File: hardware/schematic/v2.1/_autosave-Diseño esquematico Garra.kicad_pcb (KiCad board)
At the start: 2 copper layers, 85.5 x 137 mm, 26 parts

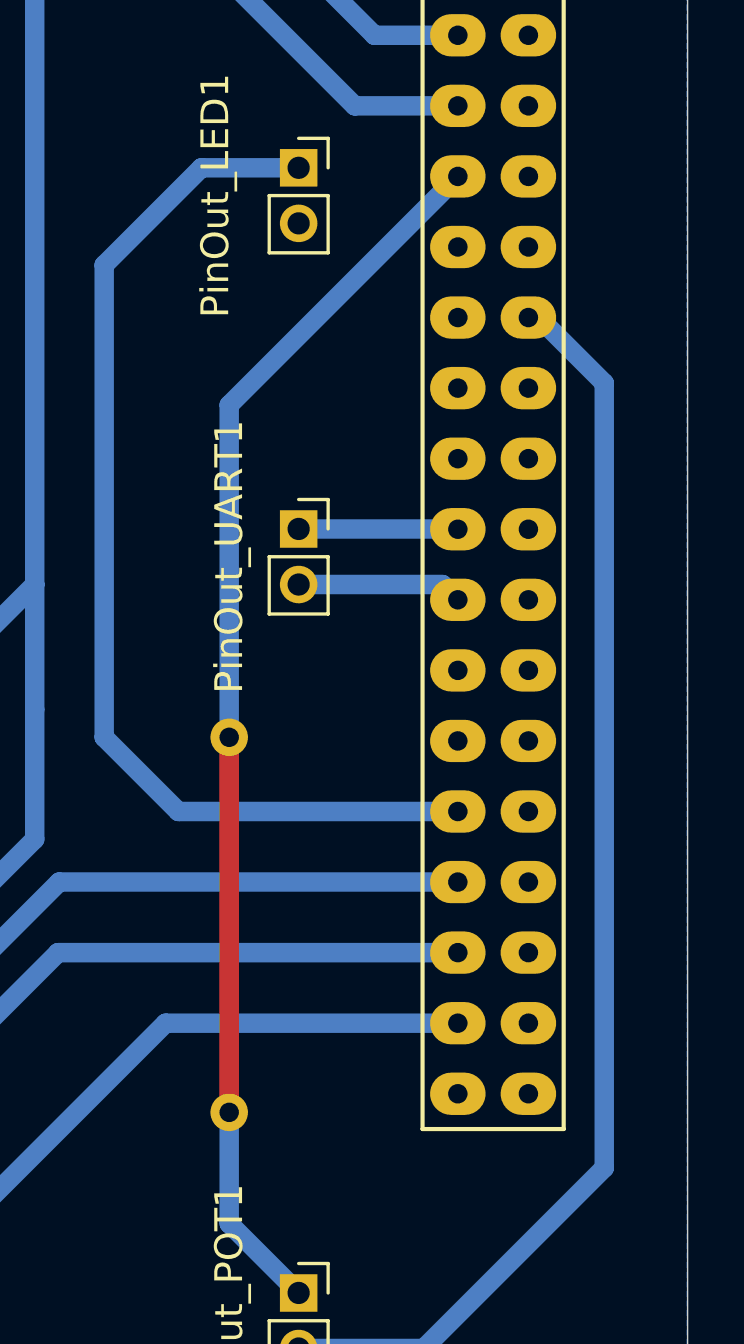
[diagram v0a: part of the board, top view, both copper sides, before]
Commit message: Pcb branch (#8)
* refactor

* feat: PCB routing first stage completed

* docs: Schematics PDF added

* fix: PCB border colision

* feat: Copper layers added to the PCB

* feat: New PCB design with new components [LED, B_M]

* feat: add through holes for connectivity & GNDs links

* feat: hole diameter adjustment

* fix: PDF

* feat: change route system in PCB

---------

Co-authored-by: ManuSavenia <saveniamanuel@egmail.com>
Co-authored-by: Iván Valentín Polanis <polanis.ivan@alu.ing.unlp.edu.ar>
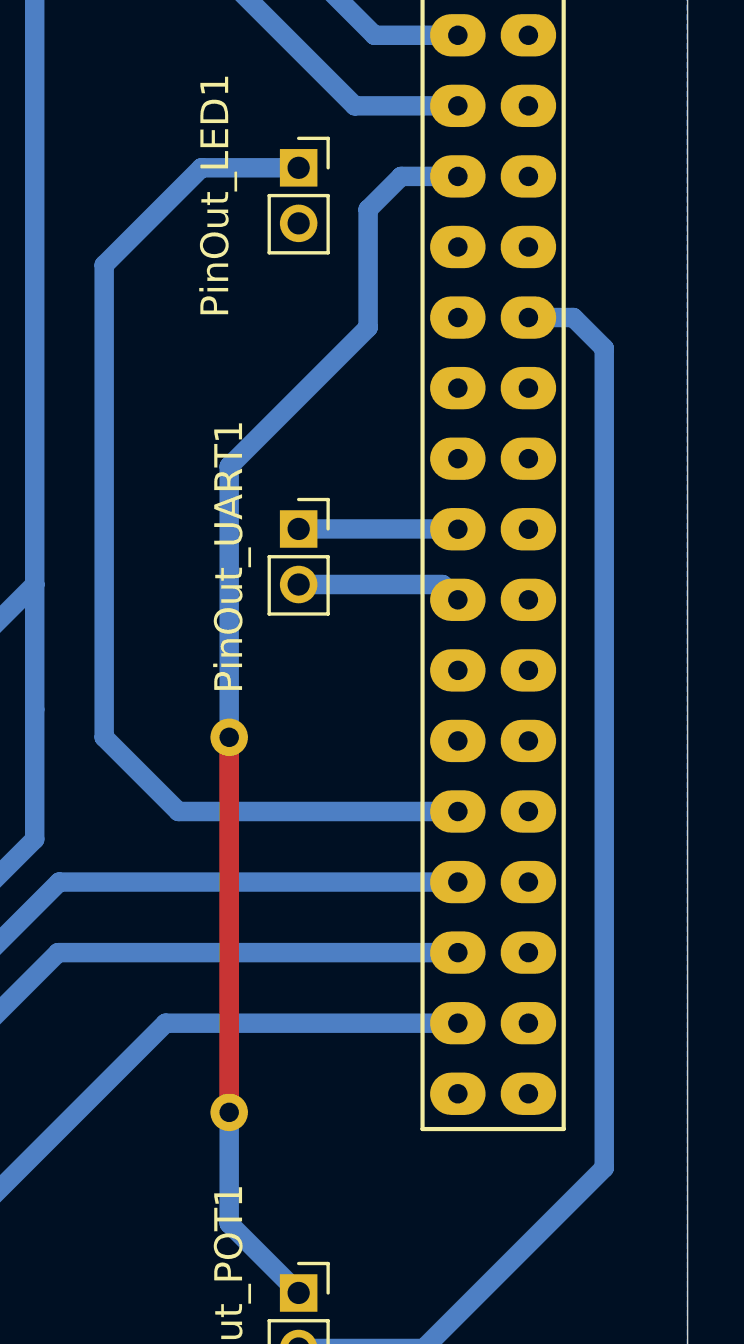
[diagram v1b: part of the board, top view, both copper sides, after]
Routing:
- net POT: track 44.6 -> 45.8 mm
- net GND_POT: track 45.6 -> 46.4 mm
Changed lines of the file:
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@@
 	(segment
 		(start 114.77 107.39)
-		(end 115.14 107.39)
-		(width 0.7)
-		(layer "B.Cu")
-		(net 15)
-	)
-	(segment
-		(start 115.14 107.39)
-		(end 117.5 109.75)
-		(width 0.7)
-		(layer "B.Cu")
-		(net 15)
-	)
-	(segment
-		(start 117.5 109.75)
-		(end 117.5 138)
+		(end 116.39 107.39)
 		(width 0.7)
 		(layer "B.Cu")
@@
 	)
 	(segment
+		(start 116.39 107.39)
+		(end 117.5 108.5)
+		(width 0.7)
+		(layer "B.Cu")
+		(net 15)
+	)
+	(segment
 		(start 111 144.5)
 		(end 106.5 144.5)
+		(width 0.7)
+		(layer "B.Cu")
+		(net 15)
+	)
+	(segment
+		(start 117.5 108.5)
+		(end 117.5 138)
 		(width 0.7)
 		(layer "B.Cu")
@@
 	)
 	(segment
-		(start 104 110.54)
+		(start 104 112.75)
+		(end 109 107.75)
+		(width 0.7)
+		(layer "B.Cu")
+		(net 17)
+	)
+	(segment
+		(start 110.19 102.31)
 		(end 112.23 102.31)
 		(width 0.7)
@@
 	)
 	(segment
-		(start 104 122.5)
-		(end 104 110.54)
+		(start 109 103.5)
+		(end 110.19 102.31)
 		(width 0.7)
 		(layer "B.Cu")
+		(net 17)
+	)
+	(segment
+		(start 109 107.75)
+		(end 109 103.5)
+		(width 0.7)
+		(layer "B.Cu")
+		(net 17)
+	)
+	(segment
+		(start 104 122.5)
+		(end 104 112.75)
+		(width 0.7)
+		(layer "B.Cu")
